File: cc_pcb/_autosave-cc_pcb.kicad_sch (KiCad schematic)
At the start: 57 parts, among them J1 Conn_02x05_Odd_Even, SW1 SW_Push, U1 LD1117S33TR_SOT223, U2 STM32F091RCTx

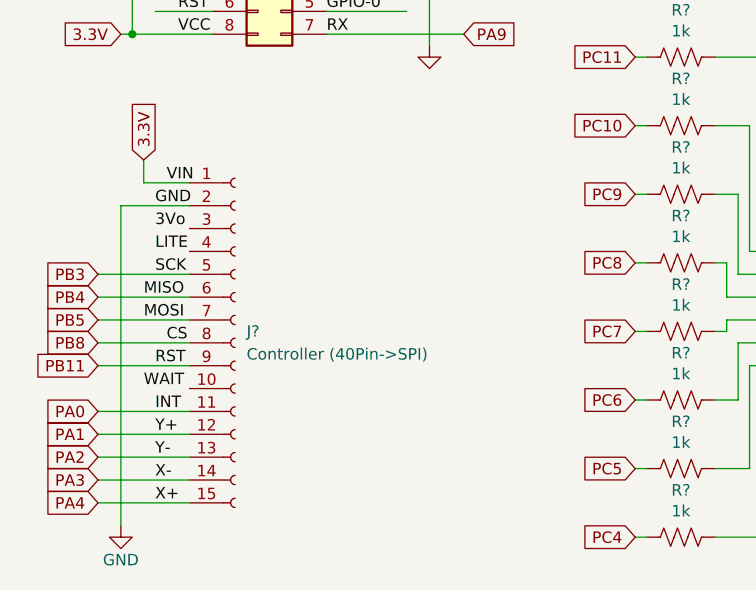
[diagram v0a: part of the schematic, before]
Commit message: linked 4x4 keypad footprint to schematic
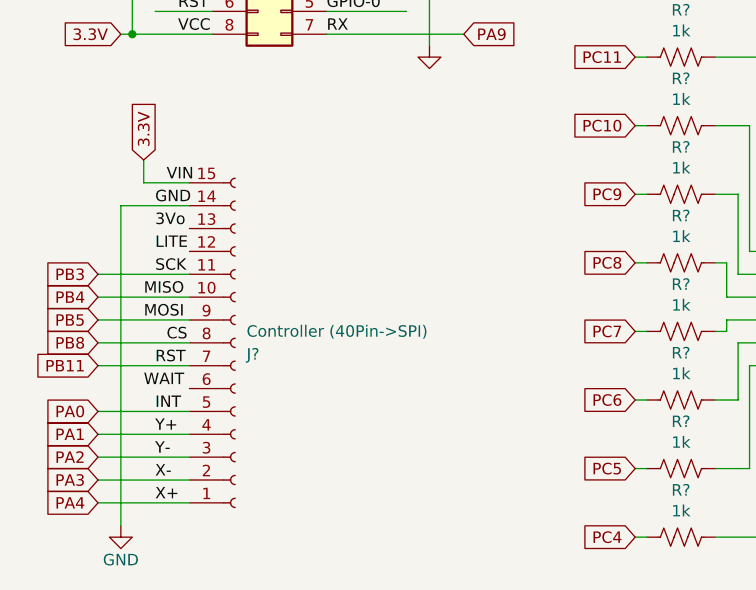
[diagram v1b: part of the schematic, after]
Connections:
- net GND: now also J?.14 (Pin_14); no longer J?.2 (Pin_2)
- net PA0: now also J?.5 (Pin_5); no longer J?.11 (Pin_11)
- net PA1: now also J?.4 (Pin_4); no longer J?.12 (Pin_12)
- net PA2: now also J?.3 (Pin_3); no longer J?.13 (Pin_13)
- net PA3: now also J?.2 (Pin_2); no longer J?.14 (Pin_14)
- net PA4: now also J?.1 (Pin_1); no longer J?.15 (Pin_15)
- net PB10: now also J?.11 (Pin_11); no longer J?.5 (Pin_5)
- net PB11: now also J?.7 (Pin_7); no longer J?.9 (Pin_9)
- net PB4: now also J?.10 (Pin_10); no longer J?.6 (Pin_6)
- net PB5: now also J?.9 (Pin_9); no longer J?.7 (Pin_7)
- net VCC: now also J?.15 (Pin_15); no longer J?.1 (Pin_1)
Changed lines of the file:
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@@
     (pin "1")
   )
-  (symbol (lib_id "Connector:Conn_01x15_Female") (at 38.1 168.91 0) (unit 1)
+  (symbol (lib_id "Connector:Conn_01x15_Female") (at 38.1 168.91 0) (mirror x) (unit 1)
     (in_bom yes) (on_board yes)
-    (property "Reference" "J?" (id 0) (at 39.37 167.6399 0)
+    (property "Reference" "J?" (id 0) (at 39.37 170.1801 0)
       (effects (font (size 1.27 1.27)) (justify left))
     )
-    (property "Value" "Controller (40Pin->SPI)" (id 1) (at 39.37 170.1799 0)
+    (property "Value" "Controller (40Pin->SPI)" (id 1) (at 39.37 167.6401 0)
       (effects (font (size 1.27 1.27)) (justify left))
     )
